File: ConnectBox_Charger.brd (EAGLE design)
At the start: 65 x 30 mm, 14 parts, among them IC1 M24C32-RDW6TP, J1 CONNECTOR_PI_40_PIN, J2 Lithium Cell, J3 microUSB Power In, J4 FTDI Serial, J5 5V Charger Output, Q1 BSS138, U1 LTC4040

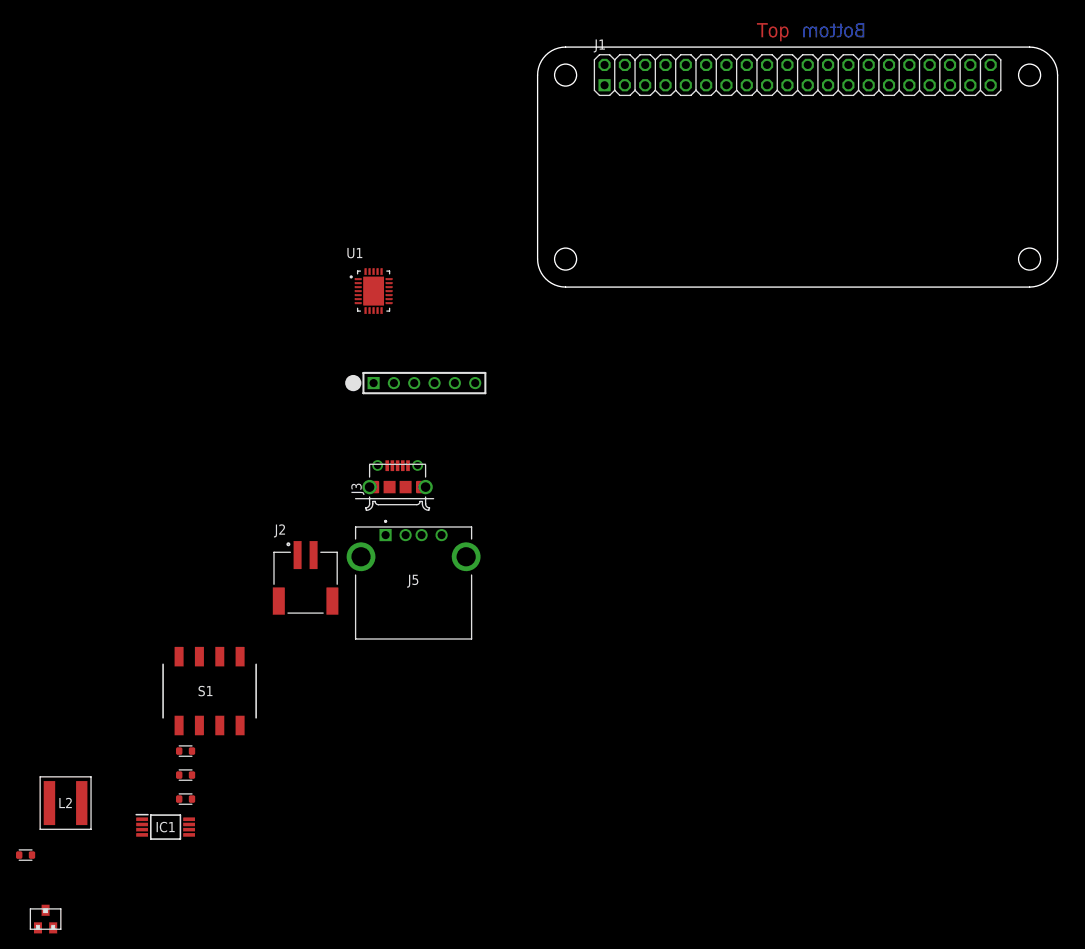
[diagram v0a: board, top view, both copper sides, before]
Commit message: almost done just need to connect the SD holder to pins
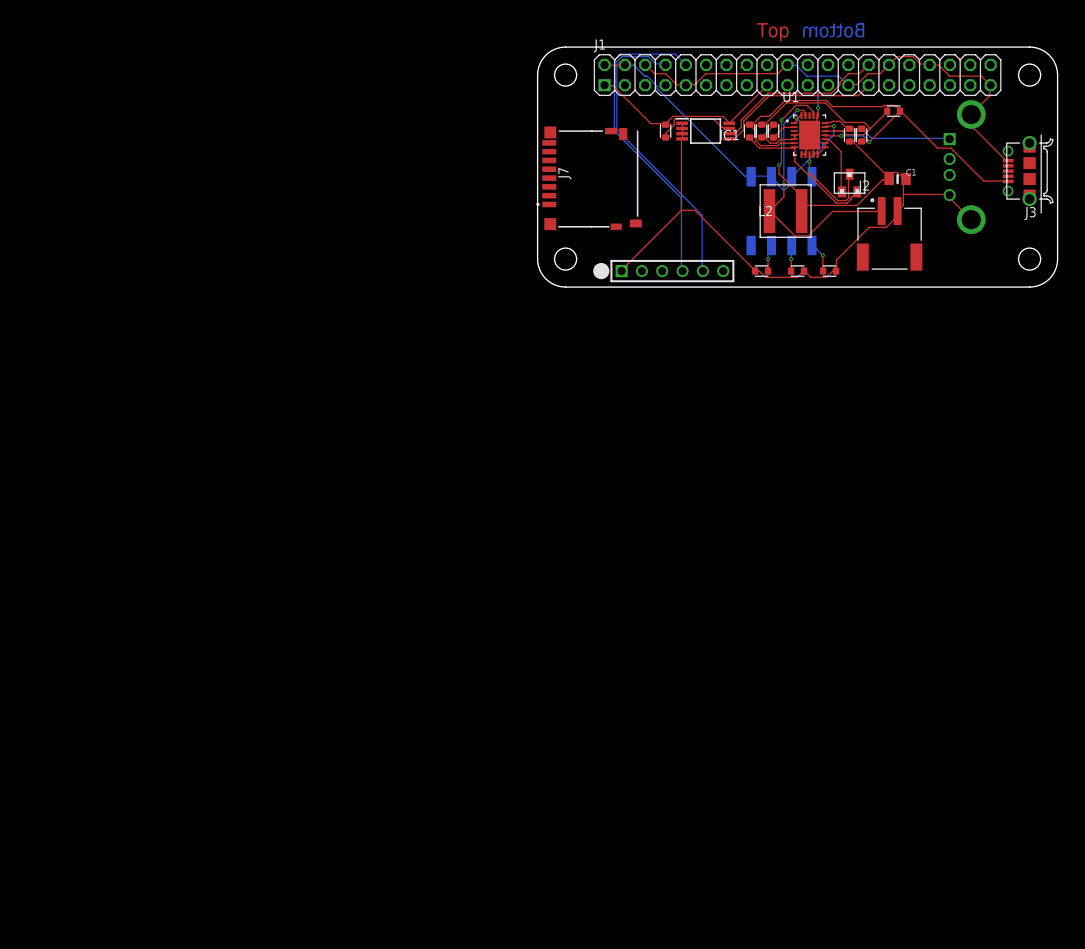
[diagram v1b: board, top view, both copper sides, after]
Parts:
- added C1: 10 uF, Adafruit LoRa Radio Bonnet with OLED:MICROBUILDER_0805_10MGAP
- added J7: 1140084168_1140084168, ConnectBox_2019:1140084168_1140084168
- added R10: 0, ConnectBox_2019:RESC1608X55L25N
- added R5: 10K, ConnectBox_2019:RESC1608X55L25N
- added R6: 60.4KR, ConnectBox_2019:RESC1608X55L25N
- added R7: 178KR, ConnectBox_2019:RESC1608X55L25N
- added R8: 2KR, ConnectBox_2019:RESC1608X55L25N
- added R9: DNP, ConnectBox_2019:RESC1608X55L25N
- R1, R2, R3: value (none) -> 10K
- moved Q1 136.3 mm to (39.0, 13.0)
- moved R4 128.0 mm to (26.5, 19.5), turned to 270 degrees
- moved L2 116.5 mm to (31.0, 9.50)
- moved IC1 110.1 mm to (21.0, 19.5)
- moved R1 100.4 mm to (36.5, 2.00), turned to 180 degrees
- moved R2 99.1 mm to (32.5, 2.00), turned to 180 degrees
- moved R3 97.7 mm to (28.0, 2.00)
- moved S1 93.3 mm to (30.5, 9.50), flipped to the bottom
- moved J3 88.3 mm to (61.5, 14.5), turned to 90 degrees
- moved J5 86.1 mm to (51.5, 18.5), flipped to the bottom, turned to 270 degrees
- moved J2 84.7 mm to (44.0, 9.50)
- moved U1 57.9 mm to (34.0, 19.0)
- moved J4 34.0 mm to (10.5, 2.00)
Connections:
- removed net V_IN: J3.1, R4.1, U1.6
- new net +3V3: IC1.8, J1.1, J1.17, R5.2
- new net ID_SCL: IC1.6, J1.28
- new net ID_SDA: IC1.5, J1.27
- new net N$3: IC1.7, R5.1
- new net N$4: R6.2, R7.2, U1.19
- new net N$5: C1.1, L2.2, U1.21, U1.22
- new net N$6: R8.1, U1.2
- new net N$9: R10.2, R9.1, U1.17
- new net VIN: J3.1, R4.1, R7.1, R9.2, U1.16, U1.6
- new net VSYS: U1.12, U1.13, U1.14
- net +5V: now also U1.10, U1.18
- net BATT: now also L2.1, U1.23
- net GND: now also C1.2, IC1.1, IC1.2, IC1.3, IC1.4, J1.20, J1.25, J1.30, J1.34, J1.39, J1.6, J1.9, R10.1, R6.1, R8.2, U1.11, U1.20, U1.8, U1.9
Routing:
- net GND: track 0.00 -> 166.7 mm, vias 0 -> 1
- net +5V: track 0.00 -> 74.4 mm, vias 0 -> 3
- net VIN: track 0.00 -> 57.9 mm, vias 0 -> 2
- net TO_PI: track 0.00 -> 39.7 mm
- net FROM_PI: track 0.00 -> 37.4 mm
- net BATT: track 0.00 -> 32.2 mm, vias 0 -> 2
- net N$5: track 0.00 -> 31.8 mm, vias 0 -> 2
- net N$9: track 0.00 -> 25.4 mm
- net +3V3: track 0.00 -> 25.3 mm
- net ID_SCL: track 0.00 -> 21.7 mm
- net ID_SDA: track 0.00 -> 20.8 mm
- net N$2: track 0.00 -> 18.7 mm
- net N$3: track 0.00 -> 10.1 mm
- net IGATE: track 0.00 -> 7.73 mm
- net N$4: track 0.00 -> 5.18 mm
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
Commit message: hopefully the last version with the charger
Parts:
- removed J7: 1140084168_1140084168, ConnectBox_2019:1140084168_1140084168
- added J6: 503182-1852, 503182-1852:MOLEX_503182-1852
- moved R5 12.3 mm to (28.2, 18.2), turned to 270 degrees
- moved L2 10.2 mm to (21.0, 11.2)
- moved Q1 9.91 mm to (31.8, 6.25), turned to 180 degrees
- moved R10 8.14 mm to (29.5, 11.5)
- moved R4 8.14 mm to (28.0, 11.5)
- moved R8 8.14 mm to (31.0, 11.5)
- moved S1 5.84 mm to (36.2, 8.50)
- moved R9 3.29 mm to (45.0, 18.8), turned to 270 degrees
- moved R6 3.01 mm to (42.0, 18.8)
- moved R7 3.01 mm to (43.5, 18.8)
- moved U1 1.95 mm to (35.5, 17.8)
- moved C1 0.90 mm to (44.2, 14.0)
- moved J2 0.56 mm to (44.2, 9.00)
- moved IC1 0.50 mm to (21.5, 19.5)
- moved J4 0.25 mm to (10.5, 2.25)
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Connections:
- new net CS: J1.24, J6.2
- new net MISO: J1.21, J6.7
- new net MOSI: J1.19, J6.3
- new net N/C: J6.1, J6.8, J6.DT
- new net SCLK: J1.23, J6.5
- net +3V3: now also J6.4
- net GND: now also J6.6, J6.P1, J6.P2, J6.P3, J6.P4, J6.P5
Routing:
- net GND: track 166.7 -> 227.1 mm, vias 1 -> 0
- net CS: track 0.00 -> 49.9 mm, vias 0 -> 1
- net SCLK: track 0.00 -> 46.2 mm, vias 0 -> 1
- net MOSI: track 0.00 -> 40.2 mm, vias 0 -> 2
- net MISO: track 0.00 -> 39.0 mm, vias 0 -> 1
- net N/C: track 0.00 -> 33.4 mm
- net +3V3: track 25.3 -> 50.1 mm, vias 0 -> 2
- net N$5: track 31.8 -> 53.9 mm, vias 2 -> 0
- net TO_PI: track 39.7 -> 26.3 mm
- net N$6: track 3.09 -> 15.6 mm
- net VIN: track 57.9 -> 46.0 mm, vias 2 -> 3
- net +5V: track 74.4 -> 83.7 mm, vias 3 -> 4
- net BATT: track 32.2 -> 41.2 mm, vias 2 -> 3
- net ID_SCL: track 21.7 -> 27.5 mm
- net FROM_PI: track 37.4 -> 31.6 mm
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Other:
- board size 65 x 30 mm -> 64.8 x 30 mm

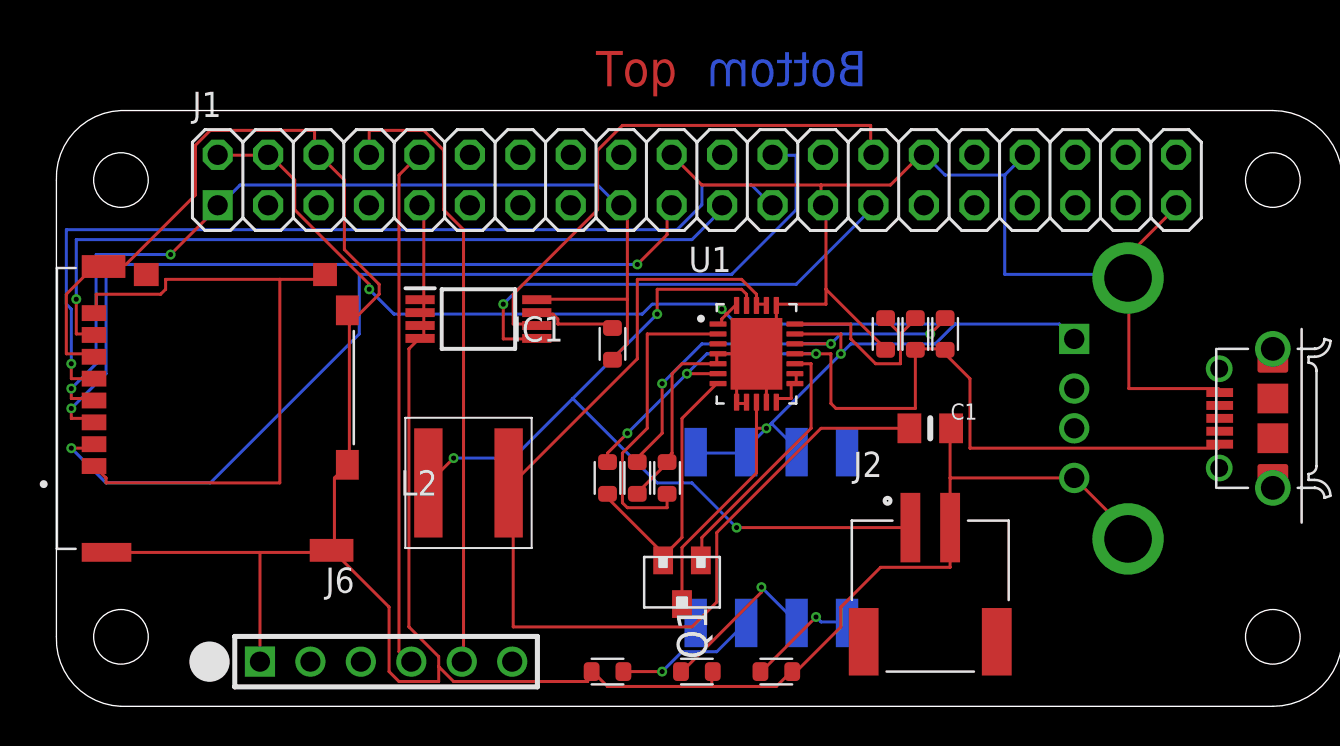
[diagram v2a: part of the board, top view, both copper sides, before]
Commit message: Final push ready for ordering as the complete charging accessory for the MAF wifi box project.PCB will connect to RaspPI0W which will distribute wifi and hold essential software.  The PCB will hold content as uploaded and desired by misionaries in the field.
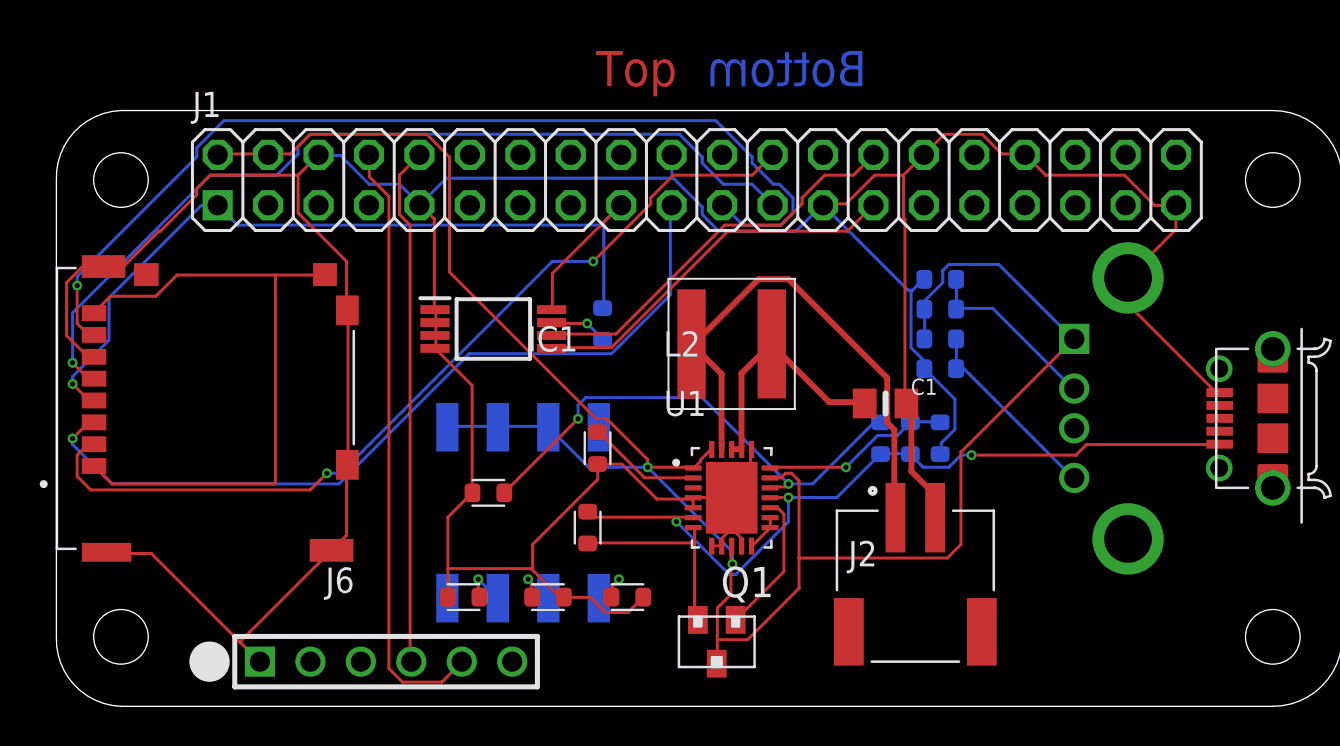
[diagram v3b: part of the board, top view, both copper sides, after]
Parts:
- added R11, R14: 49.9K 1%, ConnectBox_2019:RESC1608X55L25N
- added R12, R13: 75K 1%, ConnectBox_2019:RESC1608X55L25N
- moved L2 15.0 mm to (34.2, 18.2)
- moved S1 12.6 mm to (23.8, 9.75)
- moved R1 8.39 mm to (29.0, 5.50)
- moved R2 8.39 mm to (25.0, 5.50)
- moved R3 8.16 mm to (20.8, 5.50)
- moved R10 7.54 mm to (22.0, 10.8), turned to 0 degrees
- moved U1 7.36 mm to (34.2, 10.5)
- moved R9 6.17 mm to (41.8, 13.5), flipped to the bottom
- moved R6 5.93 mm to (44.8, 13.5), flipped to the bottom
- moved R7 5.26 mm to (43.2, 13.5), flipped to the bottom
- moved R8 3.81 mm to (27.5, 13.0), turned to 270 degrees
- moved Q1 3.47 mm to (33.5, 3.25)
- moved R4 2.69 mm to (27.0, 9.00)
- moved C1 2.57 mm to (42.0, 15.2)
- moved R5 1.12 mm to (27.8, 19.2), flipped to the bottom, turned to 90 degrees
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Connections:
- new net N$11: J5.2, R11.1, R12.1
- new net N$8: J5.4, R13.1, R14.1
- net +5V: now also R12.2, R13.2
- net GND: now also R11.2, R14.2; no longer J5.4
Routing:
- net N$5: track 53.9 -> 12.4 mm
- net +5V: track 83.7 -> 106.0 mm, vias 4 -> 2
- net GND: track 227.1 -> 209.1 mm
- net BATT: track 41.2 -> 26.4 mm, vias 3 -> 0
- net MISO: track 39.0 -> 49.8 mm
- net N$8: track 0.00 -> 9.78 mm
- net N$6: track 15.6 -> 5.86 mm
- net N$11: track 0.00 -> 9.14 mm
- net ID_SCL: track 27.5 -> 20.2 mm
- net VIN: track 46.0 -> 39.1 mm
- net F1: track 8.49 -> 2.43 mm
- net IGATE: track 13.0 -> 7.17 mm
- net CS: track 49.9 -> 44.6 mm, vias 1 -> 2
- net ID_SDA: track 24.2 -> 19.2 mm, vias 1 -> 0
- net F0: track 7.19 -> 2.37 mm
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
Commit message: hope fully final push, did not change t/b restrict or t/b keepout can change tonight if need be
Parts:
- moved J3 2.03 mm to (63.5, 14.7)
- moved J5 0.40 mm to (51.9, 18.4)
- moved J6 0.19 mm to (8.44, 14.8)
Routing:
- net GND: track 209.1 -> 304.1 mm
- net CS: track 44.6 -> 52.3 mm, vias 2 -> 1
- net MISO: track 49.8 -> 43.0 mm
- net MOSI: track 41.2 -> 38.7 mm, vias 1 -> 2
- net VIN: track 39.1 -> 41.2 mm
- net SCLK: track 44.8 -> 46.8 mm
- net +5V: track 106.0 -> 107.2 mm
- net +3V3: track 46.1 -> 46.8 mm, vias 1 -> 2
